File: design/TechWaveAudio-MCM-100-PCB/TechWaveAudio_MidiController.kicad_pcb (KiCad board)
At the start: 2 copper layers, 120.8 x 128.5 mm, 96 parts, among them J1 Control, J10 Midi, J12 PiPico2, J13 Velocity, J14 Note, J2 PowerBus, J3 Aux, J4 Gate, J5 Clock, J6 Trigger, J7 PiPico1, J9 5WaySwitch, SW1 SW_DIP_x04, U1 TL074, U2 TL074, U3 40106, U4 MCP4902, U5 MCP4725, U6 MCP4725, U7 6N137

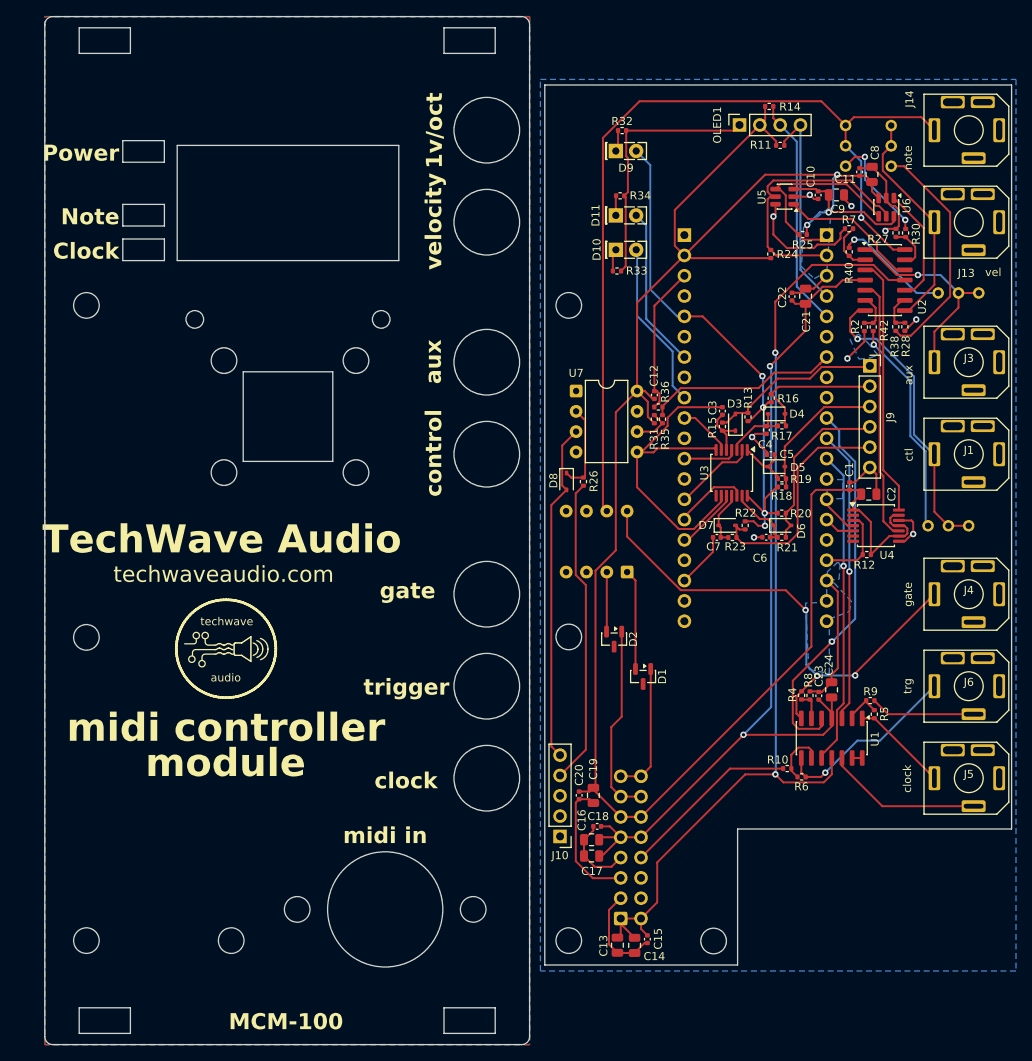
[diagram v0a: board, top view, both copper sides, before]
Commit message: move PCB and panel to separate folders
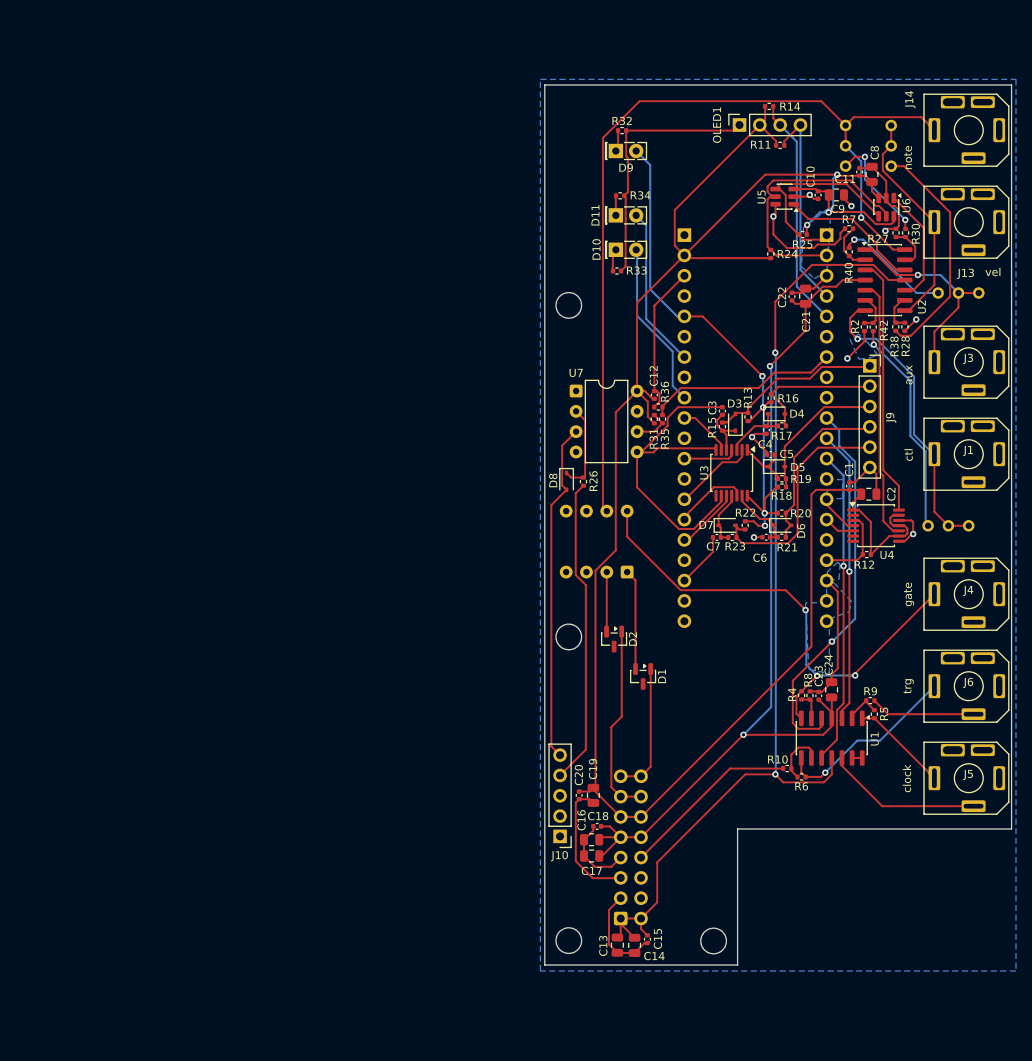
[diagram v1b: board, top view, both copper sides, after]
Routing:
- removed copper zone on B.Cu, net (none)
- removed copper zone on F.Cu, net (none)
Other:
- board size 120.8 x 128.5 mm -> 58.3 x 110 mm
- board text removed: "1v/oct"
- board text removed: "Audio Jack"
- board text removed: "Clock"
- board text removed: "MCM-100"
- board text removed: "Note"
- board text removed: "Power"
- board text removed: "TechWave Audio"
- board text removed: "control"
- board text removed: "midi controller"
- board text removed: "module"
- board text removed: "trigger"
- board text removed: "velocity"
